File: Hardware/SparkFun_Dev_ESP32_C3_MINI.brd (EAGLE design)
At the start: 17.8 x 33 mm, 64 parts, among them J1 USB Female Type C Connector, J5 Vertical Qwiic Connector, U1 ESP32-C3_MINI-1, U2 RT9080-33GJ5

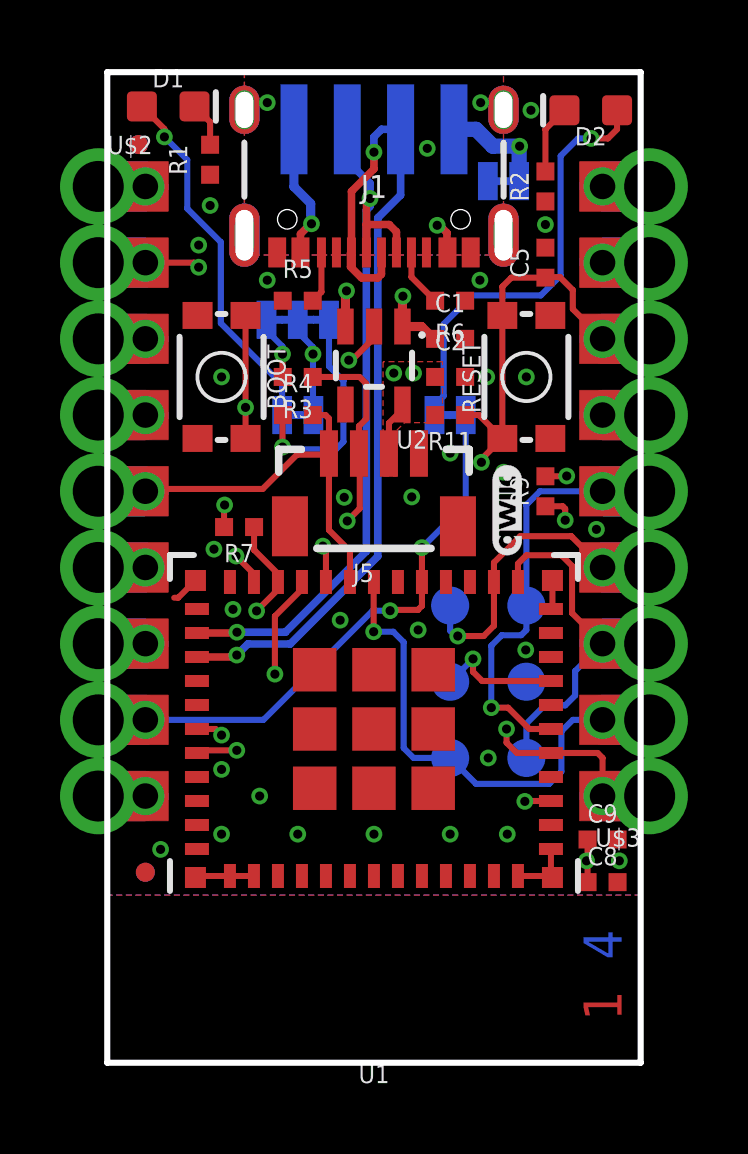
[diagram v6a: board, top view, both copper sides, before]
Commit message: Adds more silk, removes some shield polygons on inner layers
* Moves fiducials around
* Swaps I2C lines at PTH header
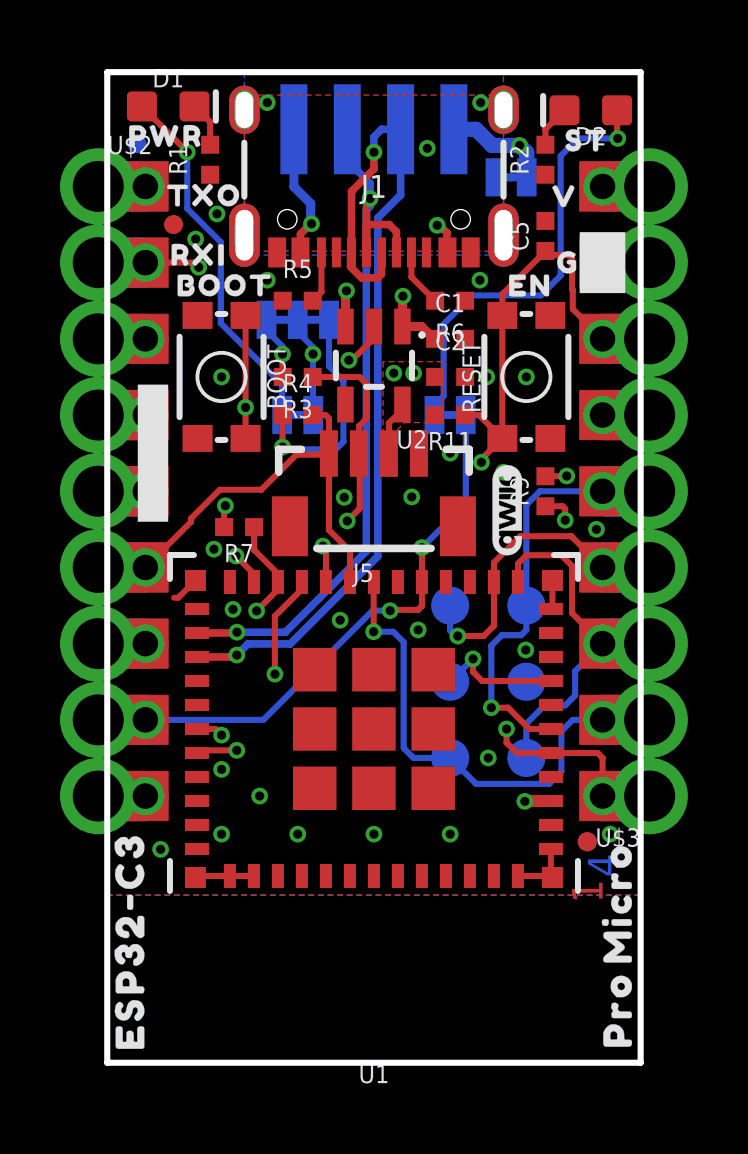
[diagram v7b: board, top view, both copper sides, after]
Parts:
- removed C8: 0.1uF, SparkFun-Capacitors:0402-TIGHT
- removed C9: 10uF, SparkFun-Capacitors:0402-TIGHT
- added U$23: (no value), prod:CK39
- added U$25: (no value), prod:D#33
- added U$26: (no value), prod:D#34
- added U$27: (no value), prod:DI36
- added U$28: (no value), prod:DO35
- added U$29: (no value), prod:EN37
- added U$30: (no value), prod:MS38
- added U$31, U$33, U$39: (no value), prod:G36
- added U$32, U$37, U$38: (no value), prod:V35
- added U$34, U$45: (no value), prod:ESP32#C32
- added U$35, U$46: (no value), prod:PRO0
- added U$36, U$47: (no value), prod:MICRO1
- added U$40: (no value), prod:EN39
- added U$41: (no value), top:BOOT15
- added U$42: (no value), prod:RXI39
- added U$43: (no value), prod:TXO40
- added U$44: (no value), top:PWR17
- added U$48: (no value), SparkFun-Aesthetics:SFE_LOGO_FLAME_.1
- added U$49: (no value), top:ST18
- U$6: device bot:#I2C#16 -> prod:#I2C#43
- U$9: device top:#SHLD#14 -> prod:#SH#44
- moved FD3 14.8 mm to (17.3, 7.37)
- moved FD4 14.8 mm to (17.3, 7.37)
- moved U$9 4.32 mm to (15.4, 31.4), turned to 270 degrees
- moved U$7 3.00 mm to (12.6, 23.1)
- moved U$8 3.00 mm to (7.62, 23.1)
- moved FD2 2.91 mm to (3.48, 27.9)
- moved U$6 2.85 mm to (10.5, 24.8)
- moved U$22 2.54 mm to (6.42, 16.4)
- moved U$21 2.49 mm to (6.62, 19.0)
- moved C5 0.89 mm to (15.9, 27.6)
- moved R2 0.89 mm to (15.9, 30.1)
- moved U$4 0.38 mm to (3.81, 22.9)
- moved SHLD 0.28 mm to (14.7, 29.5)
- moved FD1 0.06 mm to (2.26, 30.6)
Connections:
- net 3.3V: no longer C8.1, C9.1
- net GND: no longer C8.2, C9.2
- net IO5/SCL/I2S_SCK: now also U$2.4, U$2.4B; no longer U$2.5, U$2.5B
- net IO6/SDA/I2S_SDO: now also U$2.5, U$2.5B; no longer U$2.4, U$2.4B
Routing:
- net 3.3V: track 12.8 -> 7.63 mm, vias 7 -> 6
- net IO5/SCL/I2S_SCK: track 13.0 -> 14.2 mm
- net EN: track 23.4 -> 24.5 mm
- net N$3: track 2.30 -> 1.41 mm
- net GND: vias 21 -> 20
- removed copper zone on layer 15, net SHLD
- removed copper zone on layer 2, net SHLD
